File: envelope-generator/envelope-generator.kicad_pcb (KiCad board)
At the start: 2 copper layers, 60 x 77.5 mm, 32 parts, among them J1 Power, J2 Power, J3 Pot, J4 Pot, J5 Gate Input, J7 Output, SW1 Gate Button, SW2 AR/D Switch, U1 TL072

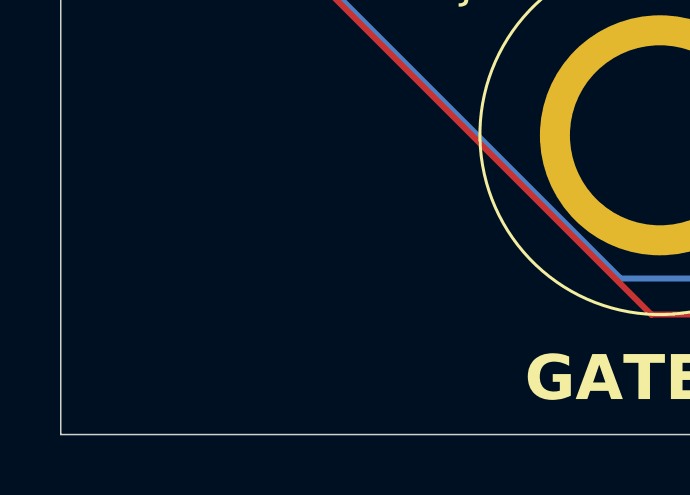
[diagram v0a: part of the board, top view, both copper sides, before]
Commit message: Add label to envelope generator
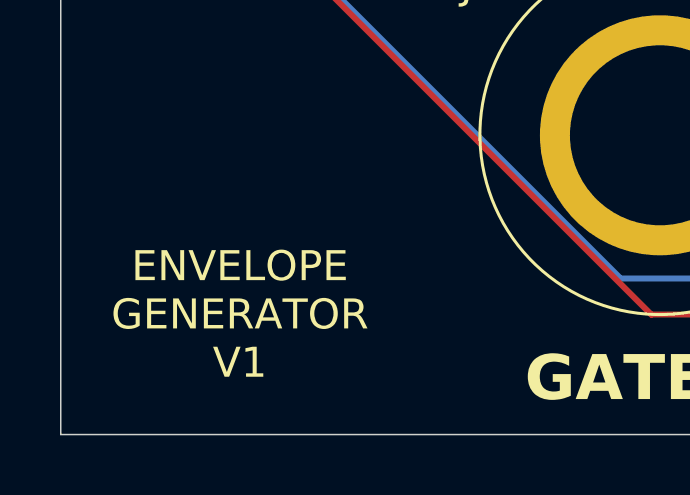
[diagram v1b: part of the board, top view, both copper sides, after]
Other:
- board text added: "ENVELOPE GENERATOR V1"
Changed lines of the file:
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@@
 			(outputformat 1)
 			(mirror no)
-			(drillshape 1)
+			(drillshape 0)
 			(scaleselection 1)
-			(outputdirectory "")
+			(outputdirectory "gerbers/")
 		)
 	)
@@
 		)
 	)
+	(gr_text "ENVELOPE\nGENERATOR\nV1"
+		(at 70 96 0)
+		(layer "F.SilkS")
+		(effects
+			(font
+				(size 1 1)
+				(thickness 0.15)
+			)
+		)
+	)

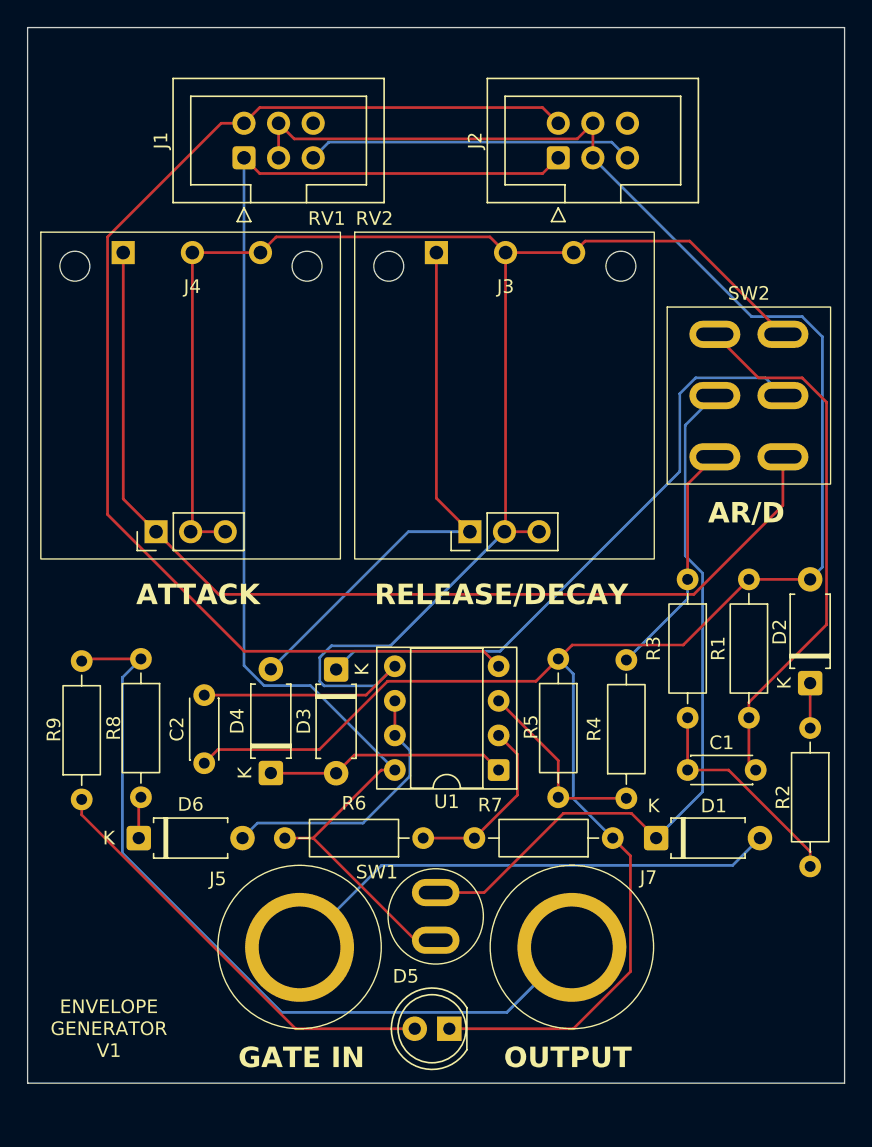
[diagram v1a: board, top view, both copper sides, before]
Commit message: More space for backup pot
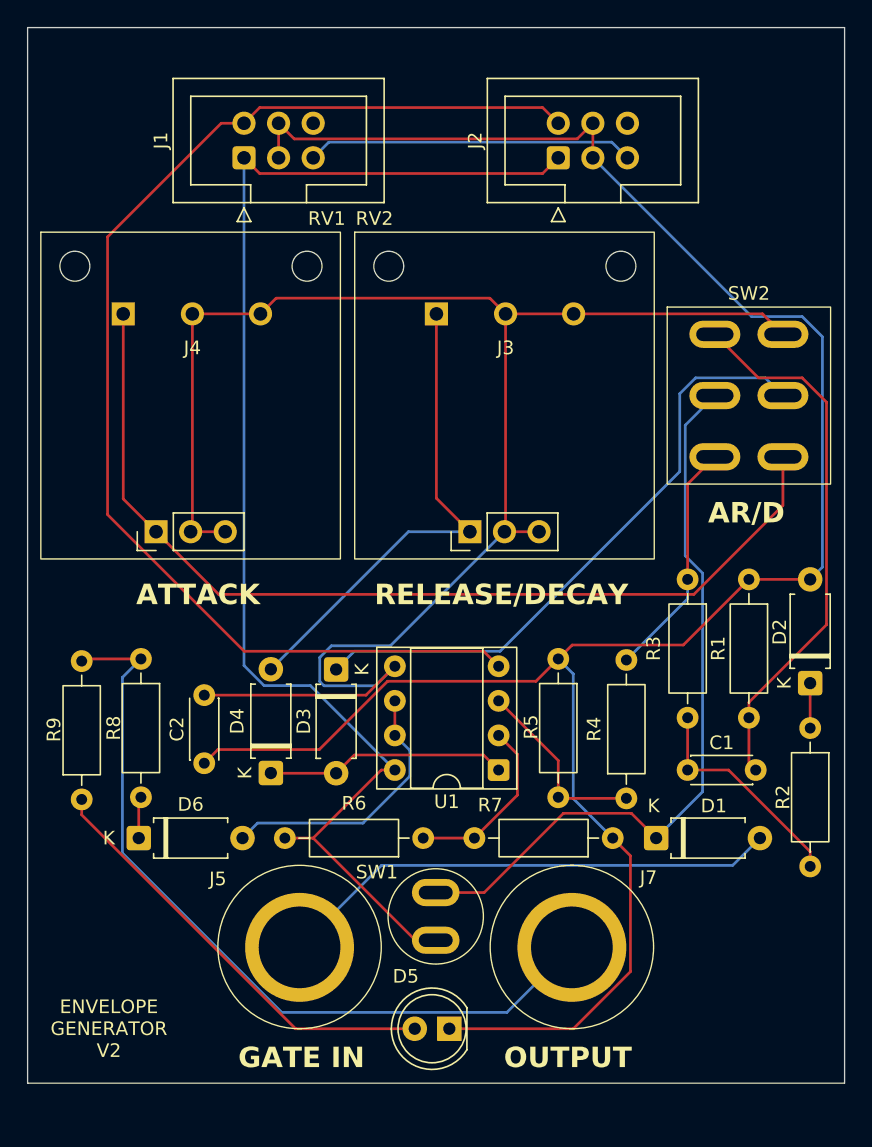
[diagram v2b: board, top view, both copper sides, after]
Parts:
- moved J3 4.50 mm to (99.1, 46.5)
- moved J4 4.50 mm to (76.1, 46.5)
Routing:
- net Net-(J3-Pin_2): track 134.0 -> 122.4 mm
- net Net-(J4-Pin_1): track 75.7 -> 71.2 mm
- net Net-(D4-A): track 40.3 -> 35.8 mm
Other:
- board text added: "ENVELOPE GENERATOR V2"
- board text removed: "ENVELOPE GENERATOR V1"
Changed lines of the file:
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@@
 	(footprint "modular2:pot"
 		(layer "F.Cu")
-		(at 99.13 42)
+		(at 99.13 46.5)
 		(property "Reference" "J3"
 			(at 0 -0.5 0)
@@
 	(footprint "modular2:pot"
 		(layer "F.Cu")
-		(at 76.13 42)
+		(at 76.13 46.5)
 		(property "Reference" "J4"
 			(at 0 -0.5 0)
@@
 		)
 	)
-	(gr_text "ENVELOPE\nGENERATOR\nV1"
+	(gr_text "ENVELOPE\nGENERATOR\nV2"
 		(at 70 96 0)
 		(layer "F.SilkS")
@@
 	)
 	(segment
-		(start 81.13 39)
-		(end 76.13 39)
-		(width 0.2)
-		(layer "F.Cu")
-		(net 4)
-	)
-	(segment
-		(start 112.65 38.15)
-		(end 119.5 45)
+		(start 82.281 42.349)
+		(end 97.979 42.349)
 		(width 0.2)
 		(layer "F.Cu")
@@
 	)
 	(segment
-		(start 99.13 39)
+		(start 99.13 43.5)
 		(end 99.13 59.42)
 		(width 0.2)
@@
 	)
 	(segment
-		(start 104.98 38.15)
-		(end 112.65 38.15)
+		(start 99.13 43.5)
+		(end 104.13 43.5)
 		(width 0.2)
 		(layer "F.Cu")
@@
 	)
 	(segment
-		(start 104.13 39)
-		(end 99.13 39)
+		(start 81.13 43.5)
+		(end 76.13 43.5)
 		(width 0.2)
 		(layer "F.Cu")
@@
 	)
 	(segment
-		(start 99.13 59.42)
-		(end 99.05 59.5)
+		(start 99.05 59.5)
+		(end 101.59 59.5)
 		(width 0.2)
 		(layer "F.Cu")
@@
 	)
 	(segment
-		(start 82.281 37.849)
-		(end 97.979 37.849)
+		(start 104.13 43.5)
+		(end 118 43.5)
 		(width 0.2)
 		(layer "F.Cu")
@@
 	)
 	(segment
-		(start 99.05 59.5)
-		(end 101.59 59.5)
+		(start 97.979 42.349)
+		(end 99.13 43.5)
 		(width 0.2)
 		(layer "F.Cu")
@@
 	)
 	(segment
-		(start 97.979 37.849)
-		(end 99.13 39)
+		(start 76.13 43.5)
+		(end 76.13 59.37)
 		(width 0.2)
 		(layer "F.Cu")
@@
 	)
 	(segment
-		(start 76.13 39)
-		(end 76.13 59.37)
+		(start 99.13 59.42)
+		(end 99.05 59.5)
 		(width 0.2)
 		(layer "F.Cu")
@@
 	)
 	(segment
-		(start 76.13 59.37)
-		(end 76 59.5)
+		(start 81.13 43.5)
+		(end 82.281 42.349)
 		(width 0.2)
 		(layer "F.Cu")
@@
 	)
 	(segment
-		(start 81.13 39)
-		(end 82.281 37.849)
+		(start 118 43.5)
+		(end 119.5 45)
 		(width 0.2)
 		(layer "F.Cu")
@@
 	)
 	(segment
-		(start 104.13 39)
-		(end 104.98 38.15)
+		(start 76.13 59.37)
+		(end 76 59.5)
 		(width 0.2)
 		(layer "F.Cu")
@@
 	)
 	(segment
-		(start 94.05 39)
+		(start 94.05 43.5)
 		(end 94.05 57.04)
 		(width 0.2)
@@
 	)
 	(segment
-		(start 71.05 57.09)
-		(end 73.46 59.5)
+		(start 78.061 64.101)
+		(end 112.95605 64.101)
 		(width 0.2)
 		(layer "F.Cu")
@@
 	)
 	(segment
-		(start 78.061 64.101)
-		(end 112.95605 64.101)
+		(start 71.05 57.09)
+		(end 73.46 59.5)
 		(width 0.2)
 		(layer "F.Cu")
@@
 	)
 	(segment
-		(start 71.05 39)
+		(start 71.05 43.5)
 		(end 71.05 57.09)
 		(width 0.2)

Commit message: Envelope generator fixes
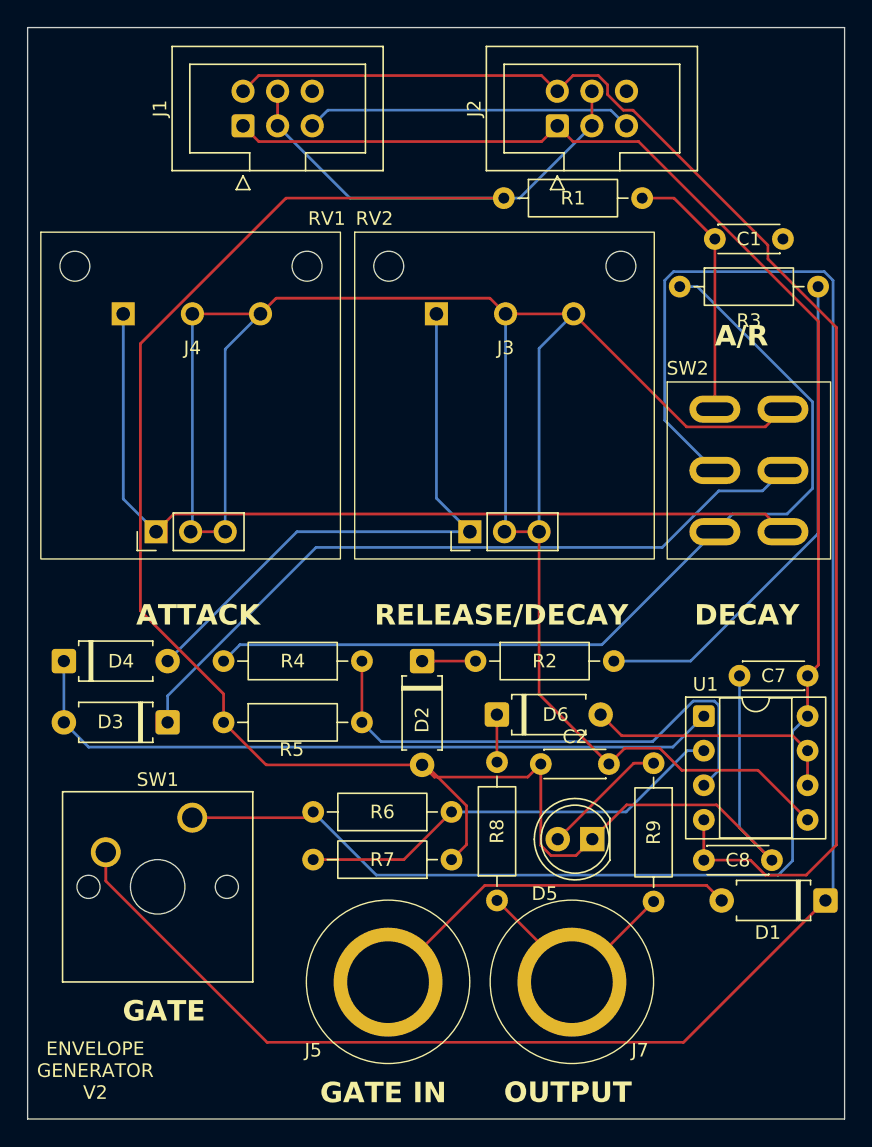
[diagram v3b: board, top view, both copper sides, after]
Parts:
- added C7: 100nF, Capacitor_THT:C_Disc_D4.3mm_W1.9mm_P5.00mm, F.Cu at (116.3, 70.1)
- added C8: 100nF, Capacitor_THT:C_Disc_D4.3mm_W1.9mm_P5.00mm, F.Cu at (118.7, 83.6)
- SW1: footprint modular2:button1 -> Button_Switch_Keyboard:SW_Cherry_MX_1.00u_PCB
- moved R9 42.1 mm to (110.0, 76.5), turned to -90 degrees
- moved C1 39.1 mm to (114.5, 38.0), turned to 0 degrees
- moved R1 33.3 mm to (99.0, 35.0), turned to 0 degrees
- moved R8 31.6 mm to (98.5, 86.6), turned to 90 degrees
- moved C2 30.1 mm to (106.7, 76.6), turned to 180 degrees
- moved D2 28.5 mm to (93.0, 69.0), turned to -90 degrees
- moved D6 27.8 mm to (98.5, 72.9)
- moved R2 25.1 mm to (96.9, 69.0), turned to 0 degrees
- moved R5 25.0 mm to (78.4, 73.5), turned to 0 degrees
- moved R4 21.9 mm to (88.6, 69.0), turned to 180 degrees
- moved R3 21.5 mm to (111.9, 41.5), turned to 0 degrees
- moved SW1 19.3 mm to (76.1, 80.5)
- moved D5 17.4 mm to (105.5, 82.1)
- moved D4 17.3 mm to (66.7, 69.0), turned to 0 degrees
- moved U1 15.6 mm to (113.7, 73.0), turned to 0 degrees
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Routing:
- net Net-(D1-K): track 54.7 -> 138.3 mm
- net Net-(SW2A-A): track 17.6 -> 68.1 mm
- net Net-(J7-Pin_1): track 59.1 -> 16.7 mm
- net 12V: track 97.8 -> 136.2 mm
- net Net-(D3-A): track 18.2 -> 53.2 mm
- net Net-(J3-Pin_2): track 122.4 -> 156.3 mm
- net Net-(U1A-+): track 13.9 -> 39.0 mm
- net Net-(D5-A): track 32.1 -> 9.35 mm
- net Net-(SW2A-C): track 39.8 -> 19.1 mm
- net Net-(C1-Pad2): track 16.4 -> 37.0 mm
- net Net-(U1A--): track 13.2 -> 32.0 mm
- net -12V: track 91.2 -> 105.8 mm
- net GND: track 159.9 -> 169.3 mm
- net Net-(D1-A): track 37.1 -> 27.9 mm
- net Net-(D3-K): track 45.6 -> 54.0 mm
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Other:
- board size 60 x 77.5 mm -> 60 x 80.2 mm
- board text added: "A/R"
- board text added: "DECAY"
- board text added: "GATE"
- board text removed: "AR/D"
- board text removed: "K"

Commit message: More envelope generator fixes
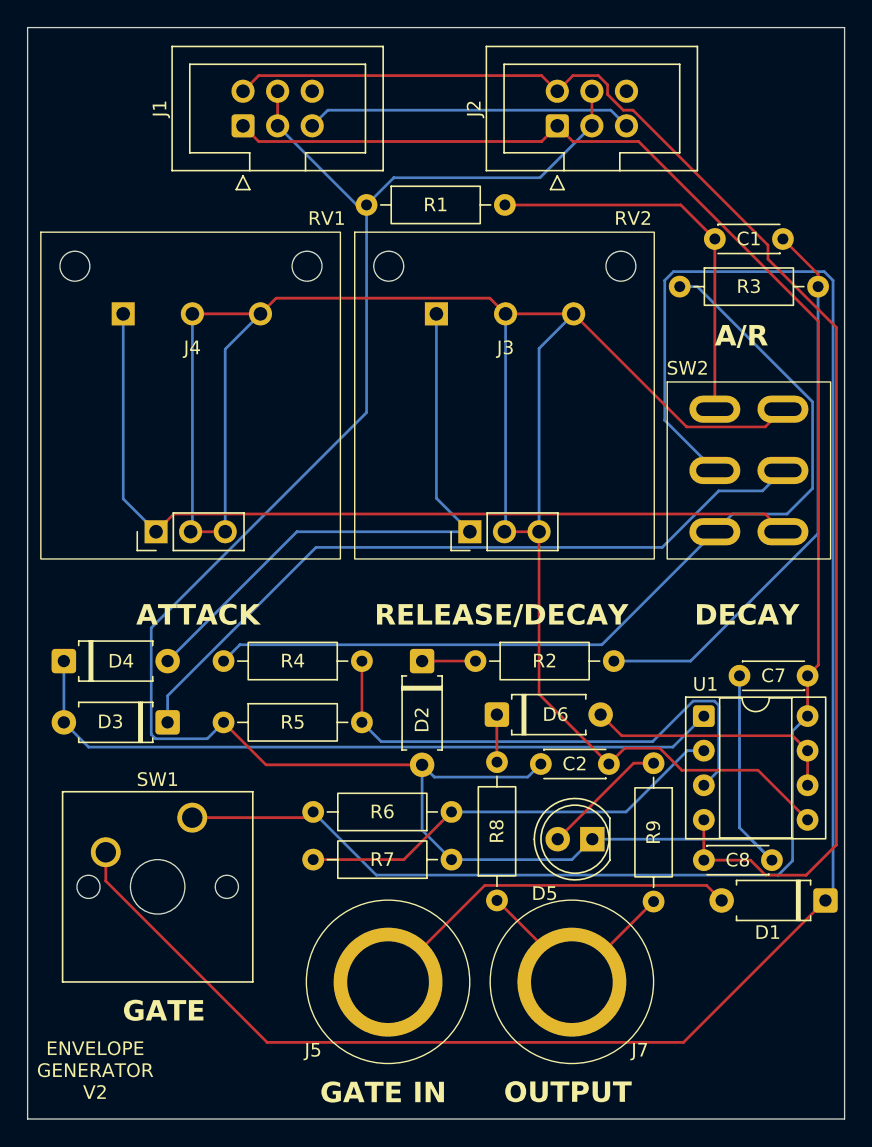
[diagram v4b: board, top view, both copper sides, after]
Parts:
- moved R1 10.1 mm to (88.9, 35.5)
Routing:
- net GND: track 169.3 -> 156.9 mm
- net Net-(SW2A-C): track 19.1 -> 29.0 mm
- net Net-(C1-Pad2): track 37.0 -> 41.6 mm
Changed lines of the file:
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@@
 		(tags "Resistor Axial_DIN0207 series Axial Horizontal pin pitch 10.16mm 0.25W = 1/4W length 6.3mm diameter 2.5mm")
 		(property "Reference" "R5"
-			(at 5 2 0)
+			(at 5.08 0 0)
 			(layer "F.SilkS")
 			(effects
@@
 		(tags "C Disc series Radial pin pitch 5.00mm diameter 4.3mm width 1.9mm Capacitor")
 		(property "Reference" "C2"
-			(at 2.5 2 0)
+			(at 2.5 0 0)
 			(layer "F.SilkS")
 			(effects
@@
 		(tags "Resistor Axial_DIN0207 series Axial Horizontal pin pitch 10.16mm 0.25W = 1/4W length 6.3mm diameter 2.5mm")
 		(property "Reference" "R3"
-			(at 5.08 2.5 0)
+			(at 5.08 0 0)
 			(layer "F.SilkS")
 			(effects
@@
 		(at 98.05 51.5)
 		(property "Reference" "RV2"
-			(at -8.55 -15 0)
+			(at 10.45 -15 0)
 			(unlocked yes)
 			(layer "F.SilkS")
@@
 	(footprint "Resistor_THT:R_Axial_DIN0207_L6.3mm_D2.5mm_P10.16mm_Horizontal"
 		(layer "F.Cu")
-		(at 99 35)
+		(at 88.92 35.5)
 		(descr "Resistor, Axial_DIN0207 series, Axial, Horizontal, pin pitch=10.16mm, 0.25W = 1/4W, length*diameter=6.3*2.5mm^2, http://cdn-reichelt.de/documents/datenblatt/B400/1_4W%23YAG.pdf")
 		(tags "Resistor Axial_DIN0207 series Axial Horizontal pin pitch 10.16mm 0.25W = 1/4W length 6.3mm diameter 2.5mm")
@@
 	)
 	(segment
+		(start 119.5 38)
+		(end 122.08 40.58)
+		(width 0.2)
+		(layer "F.Cu")
+		(net 1)
+	)
+	(segment
+		(start 122.08 40.58)
+		(end 122.08 41.5)
+		(width 0.2)
+		(layer "F.Cu")
+		(net 1)
+	)
+	(segment
 		(start 112.714892 69)
 		(end 107.08 69)
@@
 	)
 	(segment
-		(start 109.16 35)
-		(end 111.5 35)
-		(width 0.2)
-		(layer "F.Cu")
-		(net 2)
-	)
-	(segment
 		(start 114.5 38)
 		(end 114.5 50.5)
@@
 	)
 	(segment
-		(start 111.5 35)
-		(end 114.5 38)
+		(start 99.08 35.5)
+		(end 112 35.5)
 		(width 0.2)
 		(layer "F.Cu")
@@
 	)
 	(segment
-		(start 72.309 45.69324)
-		(end 72.309 65.300529)
-		(width 0.2)
-		(layer "F.Cu")
-		(net 3)
-	)
-	(segment
-		(start 78.42 71.411529)
-		(end 78.42 73.5)
-		(width 0.2)
-		(layer "F.Cu")
-		(net 3)
-	)
-	(segment
-		(start 99 35)
-		(end 83.00224 35)
+		(start 112 35.5)
+		(end 114.5 38)
 		(width 0.2)
 		(layer "F.Cu")
-		(net 3)
+		(net 2)
 	)
 	(segment
 		(start 93 76.62)
-		(end 93.25705 76.62)
+		(end 81.54 76.62)
 		(width 0.2)
 		(layer "F.Cu")
@@
 	)
 	(segment
-		(start 93 76.62)
-		(end 93.901 77.521)
+		(start 82.389 27.151)
+		(end 82.389 29.691)
 		(width 0.2)
 		(layer "F.Cu")
@@
 	)
 	(segment
-		(start 93.25705 76.62)
-		(end 96.261 79.62395)
+		(start 105.469 27.151)
+		(end 105.469 29.691)
 		(width 0.2)
 		(layer "F.Cu")
@@
 	)
 	(segment
-		(start 105.5 82.08)
-		(end 104.299 83.281)
+		(start 81.54 76.62)
+		(end 78.42 73.5)
 		(width 0.2)
 		(layer "F.Cu")
@@
 	)
 	(segment
-		(start 114.631207 79.559)
-		(end 108.021 79.559)
+		(start 95.16 83.58)
+		(end 93 81.42)
 		(width 0.2)
-		(layer "F.Cu")
+		(layer "B.Cu")
 		(net 3)
 	)
 	(segment
-		(start 101.719351 82.537822)
-		(end 101.719351 76.559953)
+		(start 73.42484 74.701)
+		(end 77.219 74.701)
 		(width 0.2)
-		(layer "F.Cu")
+		(layer "B.Cu")
 		(net 3)
 	)
 	(segment
-		(start 100.758304 77.521)
-		(end 101.719351 76.559953)
+		(start 88.92 50.74776)
+		(end 73.109 66.55876)
 		(width 0.2)
-		(layer "F.Cu")
+		(layer "B.Cu")
 		(net 3)
 	)
 	(segment
-		(start 118.691655 83.619448)
-		(end 114.631207 79.559)
+		(start 88.92 35.5)
+		(end 90.92 33.5)
 		(width 0.2)
-		(layer "F.Cu")
+		(layer "B.Cu")
 		(net 3)
 	)
 	(segment
-		(start 105.469 27.151)
-		(end 105.469 29.691)
+		(start 77.219 74.701)
+		(end 78.42 73.5)
 		(width 0.2)
-		(layer "F.Cu")
+		(layer "B.Cu")
 		(net 3)
 	)
 	(segment
-		(start 93.901 77.521)
-		(end 100.758304 77.521)
+		(start 105.5 82.08)
+		(end 104 83.58)
 		(width 0.2)
-		(layer "F.Cu")
+		(layer "B.Cu")
 		(net 3)
 	)
 	(segment
-		(start 81.54 76.62)
-		(end 78.42 73.5)
+		(start 90.92 33.5)
+		(end 101.66 33.5)
 		(width 0.2)
-		(layer "F.Cu")
+		(layer "B.Cu")
 		(net 3)
 	)
 	(segment
-		(start 72.309 65.300529)
-		(end 78.42 71.411529)
+		(start 88.198 35.5)
+		(end 88.92 35.5)
 		(width 0.2)
-		(layer "F.Cu")
+		(layer "B.Cu")
 		(net 3)
 	)
 	(segment
-		(start 104.299 83.281)
-		(end 102.462529 83.281)
+		(start 101.66 33.5)
+		(end 105.469 29.691)
 		(width 0.2)
-		(layer "F.Cu")
+		(layer "B.Cu")
 		(net 3)
 	)
 	(segment
-		(start 96.261 82.479)
-		(end 95.16 83.58)
+		(start 73.109 66.55876)
+		(end 73.109 74.38516)
 		(width 0.2)
-		(layer "F.Cu")
+		(layer "B.Cu")
 		(net 3)
 	)
 	(segment
-		(start 93 76.62)
-		(end 81.54 76.62)
+		(start 118.691655 83.619448)
+		(end 117.152207 82.08)
 		(width 0.2)
-		(layer "F.Cu")
+		(layer "B.Cu")
 		(net 3)
 	)
 	(segment
-		(start 108.021 79.559)
-		(end 105.5 82.08)
+		(start 93.901 77.521)
+		(end 93 76.62)
 		(width 0.2)
-		(layer "F.Cu")
+		(layer "B.Cu")
 		(net 3)
 	)
 	(segment
-		(start 83.00224 35)
-		(end 72.309 45.69324)
+		(start 93 81.42)
+		(end 93 76.62)
 		(width 0.2)
-		(layer "F.Cu")
+		(layer "B.Cu")
 		(net 3)
 	)
 	(segment
-		(start 82.389 27.151)
-		(end 82.389 29.691)
+		(start 116.31 70.08)
+		(end 116.31 81.237793)
 		(width 0.2)
-		(layer "F.Cu")
+		(layer "B.Cu")
 		(net 3)
 	)
 	(segment
-		(start 102.462529 83.281)
-		(end 101.719351 82.537822)
+		(start 82.389 29.691)
+		(end 88.198 35.5)
 		(width 0.2)
-		(layer "F.Cu")
+		(layer "B.Cu")
 		(net 3)
 	)
 	(segment
-		(start 96.261 79.62395)
-		(end 96.261 82.479)
+		(start 104 83.58)
+		(end 95.16 83.58)
 		(width 0.2)
-		(layer "F.Cu")
+		(layer "B.Cu")
 		(net 3)
 	)
 	(segment
-		(start 82.389 29.691)
-		(end 87.698 35)
+		(start 101.719351 76.559953)
+		(end 100.758304 77.521)
 		(width 0.2)
 		(layer "B.Cu")
@@
 	)
 	(segment
-		(start 116.31 81.237793)
-		(end 118.691655 83.619448)
+		(start 100.758304 77.521)
+		(end 93.901 77.521)
 		(width 0.2)
 		(layer "B.Cu")
@@
 	)
 	(segment
-		(start 105.469 29.691)
-		(end 100.16 35)
+		(start 117.152207 82.08)
+		(end 105.5 82.08)
 		(width 0.2)
 		(layer "B.Cu")
@@
 	)
 	(segment
-		(start 116.31 70.08)
-		(end 116.31 81.237793)
+		(start 116.31 81.237793)
+		(end 118.691655 83.619448)
 		(width 0.2)
 		(layer "B.Cu")
@@
 	)
 	(segment
-		(start 100.16 35)
-		(end 99 35)
+		(start 73.109 74.38516)
+		(end 73.42484 74.701)
 		(width 0.2)
 		(layer "B.Cu")
@@
 	)
 	(segment
-		(start 87.698 35)
-		(end 99 35)
+		(start 88.92 35.5)
+		(end 88.92 50.74776)
 		(width 0.2)
 		(layer "B.Cu")
@@
 	)
 	(segment
-		(start 99.13 59.42)
-		(end 99.05 59.5)
-		(width 0.2)
-		(layer "F.Cu")
-		(net 4)
-	)
-	(segment
 		(start 81.13 43.5)
 		(end 82.281 42.349)
 		(width 0.2)
 		(layer "F.Cu")
-		(net 4)
-	)
-	(segment
-		(start 76.13 59.37)
-		(end 76 59.5)
-		(width 0.2)
-		(layer "F.Cu")

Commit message: Various improvements
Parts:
- added G***: LOGO, modular2:ibis-small, F.Cu at (120.0, 97.5)
- renumbered C7 to C3, C8 to C4
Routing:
- net Net-(C1-Pad2): track 41.6 -> 42.8 mm
- net Net-(J3-Pin_2): track 156.0 -> 156.8 mm
- net Net-(J4-Pin_1): track 64.1 -> 64.7 mm
